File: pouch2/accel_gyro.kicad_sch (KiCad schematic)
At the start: 15 parts, among them U2 BME688, U3 BME280

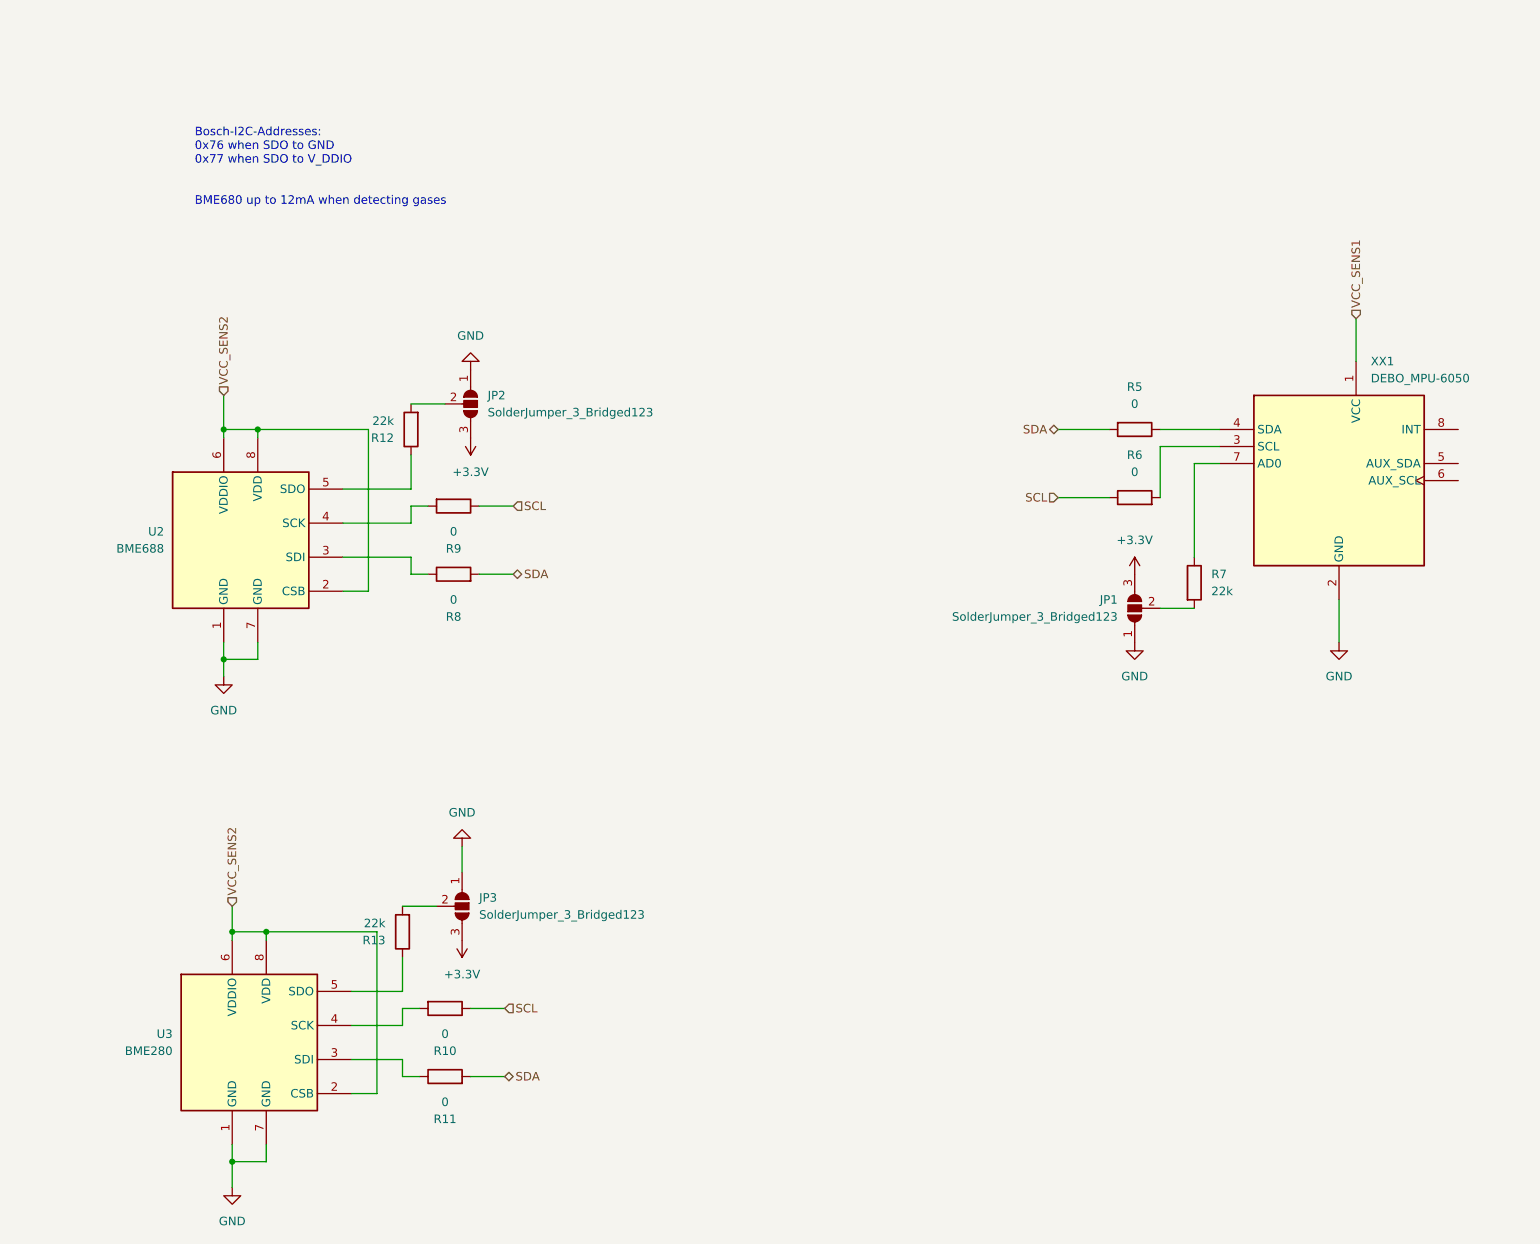
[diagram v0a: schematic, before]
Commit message: added power, sdcard
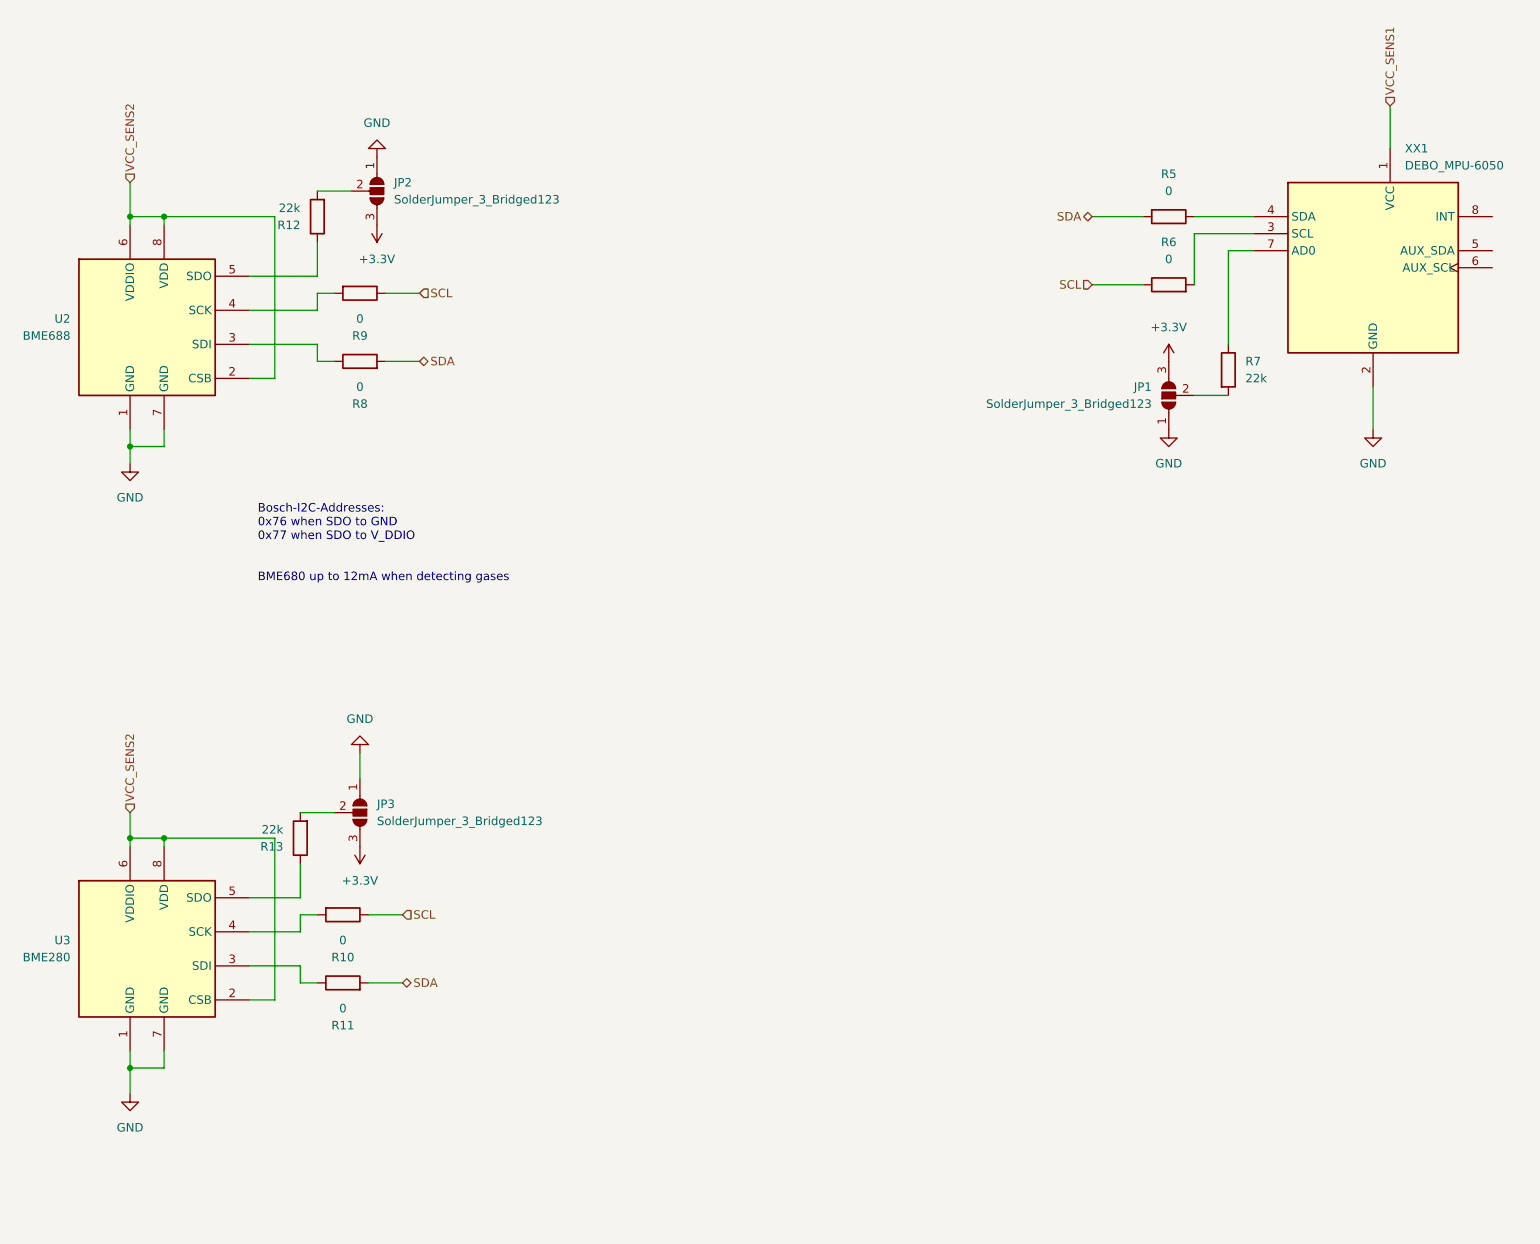
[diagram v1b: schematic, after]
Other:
- moved on the sheet: JP1, JP2, JP3, R10, R11, R12, R13, R5, R6, R7, R8, R9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

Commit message: added pi zero header
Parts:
- JP1, JP2, JP3: footprint (none) -> Jumper:SolderJumper-3_P2.0mm_Open_TrianglePad1.0x1.5mm_NumberLabels
- R10, R11, R12, R13, R5, R6, R7, R8, R9: footprint (none) -> Resistor_SMD:R_0815_2038Metric
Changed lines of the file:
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@@
 			)
 		)
-		(property "Footprint" ""
+		(property "Footprint" "Resistor_SMD:R_0815_2038Metric"
 			(at 71.12 143.002 90)
 			(effects
@@
 			)
 		)
-		(property "Footprint" ""
+		(property "Footprint" "Jumper:SolderJumper-3_P2.0mm_Open_TrianglePad1.0x1.5mm_NumberLabels"
 			(at 73.66 129.54 0)
 			(effects
@@
 			)
 		)
-		(property "Footprint" ""
+		(property "Footprint" "Jumper:SolderJumper-3_P2.0mm_Open_TrianglePad1.0x1.5mm_NumberLabels"
 			(at 194.31 67.31 0)
 			(effects
@@
 			)
 		)
-		(property "Footprint" ""
+		(property "Footprint" "Resistor_SMD:R_0815_2038Metric"
 			(at 194.31 52.578 90)
 			(effects
@@
 			)
 		)
-		(property "Footprint" ""
+		(property "Footprint" "Resistor_SMD:R_0815_2038Metric"
 			(at 71.12 156.718 90)
 			(effects
@@
 			)
 		)
-		(property "Footprint" ""
+		(property "Footprint" "Jumper:SolderJumper-3_P2.0mm_Open_TrianglePad1.0x1.5mm_NumberLabels"
 			(at 76.2 36.83 0)
 			(effects
@@
 			)
 		)
-		(property "Footprint" ""
+		(property "Footprint" "Resistor_SMD:R_0815_2038Metric"
 			(at 73.66 64.008 90)
 			(effects
@@
 			)
 		)
-		(property "Footprint" ""
+		(property "Footprint" "Resistor_SMD:R_0815_2038Metric"
 			(at 69.088 40.64 90)
 			(effects
@@
 			)
 		)
-		(property "Footprint" ""
+		(property "Footprint" "Resistor_SMD:R_0815_2038Metric"
 			(at 73.66 50.292 90)
 			(effects
@@
 			)
 		)
-		(property "Footprint" ""
+		(property "Footprint" "Resistor_SMD:R_0815_2038Metric"
 			(at 194.31 38.862 90)
 			(effects
@@
 			)
 		)
-		(property "Footprint" ""
+		(property "Footprint" "Resistor_SMD:R_0815_2038Metric"
 			(at 66.548 133.35 90)
 			(effects
@@
 			)
 		)
-		(property "Footprint" ""
+		(property "Footprint" "Resistor_SMD:R_0815_2038Metric"
 			(at 201.422 63.5 90)
 			(effects

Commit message: started PCB design
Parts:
- R201: renamed from R13; footprint Resistor_SMD:R_0815_2038Metric -> Resistor_SMD:R_0805_2012Metric
- R202: renamed from R12; footprint Resistor_SMD:R_0815_2038Metric -> Resistor_SMD:R_0805_2012Metric
- R203: renamed from R10; footprint Resistor_SMD:R_0815_2038Metric -> Resistor_SMD:R_0805_2012Metric
- R204: renamed from R11; footprint Resistor_SMD:R_0815_2038Metric -> Resistor_SMD:R_0805_2012Metric
- R205: renamed from R9; footprint Resistor_SMD:R_0815_2038Metric -> Resistor_SMD:R_0805_2012Metric
- R206: renamed from R8; footprint Resistor_SMD:R_0815_2038Metric -> Resistor_SMD:R_0805_2012Metric
- R207: renamed from R5; footprint Resistor_SMD:R_0815_2038Metric -> Resistor_SMD:R_0805_2012Metric
- R208: renamed from R6; footprint Resistor_SMD:R_0815_2038Metric -> Resistor_SMD:R_0805_2012Metric
- R209: renamed from R7; footprint Resistor_SMD:R_0815_2038Metric -> Resistor_SMD:R_0805_2012Metric
- renumbered JP3 to JP201, JP2 to JP202, JP1 to JP203, U2 to U201, U3 to U202, XX1 to XX201
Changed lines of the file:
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@@
 		(dnp no)
 		(fields_autoplaced yes)
-		(property "Reference" "R10"
+		(property "Reference" "R203"
 			(at 71.12 151.13 90)
 			(effects
@@
 			)
 		)
-		(property "Footprint" "Resistor_SMD:R_0815_2038Metric"
+		(property "Footprint" "Resistor_SMD:R_0805_2012Metric"
 			(at 71.12 143.002 90)
 			(effects
@@
 			(project "pouch2"
 				(path "/278cfa6b-9496-4a22-b425-8abdb96793ef/245dc3ad-3701-4382-b188-f6e1df98764a"
-					(reference "R10")
+					(reference "R203")
 					(unit 1)
 				)
@@
 		(dnp no)
 		(fields_autoplaced yes)
-		(property "Reference" "JP3"
+		(property "Reference" "JP201"
 			(at 76.2 128.2699 90)
 			(effects
@@
 			(project "pouch2"
 				(path "/278cfa6b-9496-4a22-b425-8abdb96793ef/245dc3ad-3701-4382-b188-f6e1df98764a"
-					(reference "JP3")
+					(reference "JP201")
 					(unit 1)
 				)
@@
 		(dnp no)
 		(fields_autoplaced yes)
-		(property "Reference" "#PWR012"
+		(property "Reference" "#PWR0204"
 			(at 73.66 130.81 0)
 			(effects
@@
 			(project "pouch2"
 				(path "/278cfa6b-9496-4a22-b425-8abdb96793ef/245dc3ad-3701-4382-b188-f6e1df98764a"
-					(reference "#PWR012")
+					(reference "#PWR0204")
 					(unit 1)
 				)
@@
 		(dnp no)
 		(fields_autoplaced yes)
-		(property "Reference" "JP1"
+		(property "Reference" "JP203"
 			(at 191.77 66.0399 90)
 			(effects
@@
 			(project "pouch2"
 				(path "/278cfa6b-9496-4a22-b425-8abdb96793ef/245dc3ad-3701-4382-b188-f6e1df98764a"
-					(reference "JP1")
+					(reference "JP203")
 					(unit 1)
 				)
@@
 		(dnp no)
 		(fields_autoplaced yes)
-		(property "Reference" "#PWR02"
+		(property "Reference" "#PWR0208"
 			(at 194.31 78.74 0)
 			(effects
@@
 			(project "pouch2"
 				(path "/278cfa6b-9496-4a22-b425-8abdb96793ef/245dc3ad-3701-4382-b188-f6e1df98764a"
-					(reference "#PWR02")
+					(reference "#PWR0208")
 					(unit 1)
 				)
@@
 		(dnp no)
 		(fields_autoplaced yes)
-		(property "Reference" "R6"
+		(property "Reference" "R208"
 			(at 194.31 44.45 90)
 			(effects
@@
 			)
 		)
-		(property "Footprint" "Resistor_SMD:R_0815_2038Metric"
+		(property "Footprint" "Resistor_SMD:R_0805_2012Metric"
 			(at 194.31 52.578 90)
 			(effects
@@
 			(project "pouch2"
 				(path "/278cfa6b-9496-4a22-b425-8abdb96793ef/245dc3ad-3701-4382-b188-f6e1df98764a"
-					(reference "R6")
+					(reference "R208")
 					(unit 1)
 				)
@@
 		(dnp no)
 		(fields_autoplaced yes)
-		(property "Reference" "U2"
+		(property "Reference" "U201"
 			(at 30.48 55.8799 0)
 			(effects
@@
 			(project ""
 				(path "/278cfa6b-9496-4a22-b425-8abdb96793ef/245dc3ad-3701-4382-b188-f6e1df98764a"
-					(reference "U2")
+					(reference "U201")
 					(unit 1)
 				)
@@
 		(dnp no)
 		(fields_autoplaced yes)
-		(property "Reference" "R11"
+		(property "Reference" "R204"
 			(at 71.12 161.29 90)
 			(effects
@@
 			)
 		)
-		(property "Footprint" "Resistor_SMD:R_0815_2038Metric"
+		(property "Footprint" "Resistor_SMD:R_0805_2012Metric"
 			(at 71.12 156.718 90)
 			(effects
@@
 			(project "pouch2"
 				(path "/278cfa6b-9496-4a22-b425-8abdb96793ef/245dc3ad-3701-4382-b188-f6e1df98764a"
-					(reference "R11")
+					(reference "R204")
 					(unit 1)
 				)
@@
 		(dnp no)
 		(fields_autoplaced yes)
-		(property "Reference" "#PWR05"
+		(property "Reference" "#PWR0209"
 			(at 224.79 78.74 0)
 			(effects
@@
 			(project "pouch2"
 				(path "/278cfa6b-9496-4a22-b425-8abdb96793ef/245dc3ad-3701-4382-b188-f6e1df98764a"
-					(reference "#PWR05")
+					(reference "#PWR0209")
 					(unit 1)
 				)
@@
 		(dnp no)
 		(fields_autoplaced yes)
-		(property "Reference" "JP2"
+		(property "Reference" "JP202"
 			(at 78.74 35.5599 90)
 			(effects
@@
 			(project "pouch2"
 				(path "/278cfa6b-9496-4a22-b425-8abdb96793ef/245dc3ad-3701-4382-b188-f6e1df98764a"
-					(reference "JP2")
+					(reference "JP202")
 					(unit 1)
 				)
@@
 		(dnp no)
 		(fields_autoplaced yes)
-		(property "Reference" "XX1"
+		(property "Reference" "XX201"
 			(at 229.5241 30.48 0)
 			(effects
@@
 			(project "pouch2"
 				(path "/278cfa6b-9496-4a22-b425-8abdb96793ef/245dc3ad-3701-4382-b188-f6e1df98764a"
-					(reference "XX1")
+					(reference "XX201")
 					(unit 1)
 				)
@@
 		(dnp no)
 		(fields_autoplaced yes)
-		(property "Reference" "#PWR011"
+		(property "Reference" "#PWR0203"
 			(at 73.66 114.3 0)
 			(effects
@@
 			(project "pouch2"
 				(path "/278cfa6b-9496-4a22-b425-8abdb96793ef/245dc3ad-3701-4382-b188-f6e1df98764a"
-					(reference "#PWR011")
+					(reference "#PWR0203")
 					(unit 1)
 				)
@@
 		(dnp no)
 		(fields_autoplaced yes)
-		(property "Reference" "R8"
+		(property "Reference" "R206"
 			(at 73.66 68.58 90)
 			(effects
@@
 			)
 		)
-		(property "Footprint" "Resistor_SMD:R_0815_2038Metric"
+		(property "Footprint" "Resistor_SMD:R_0805_2012Metric"
 			(at 73.66 64.008 90)
 			(effects
@@
 			(project "pouch2"
 				(path "/278cfa6b-9496-4a22-b425-8abdb96793ef/245dc3ad-3701-4382-b188-f6e1df98764a"
-					(reference "R8")
+					(reference "R206")
 					(unit 1)
 				)
@@
 		(dnp no)
 		(fields_autoplaced yes)
-		(property "Reference" "R12"
+		(property "Reference" "R202"
 			(at 64.77 41.9101 0)
 			(effects
@@
 			)
 		)
-		(property "Footprint" "Resistor_SMD:R_0815_2038Metric"
+		(property "Footprint" "Resistor_SMD:R_0805_2012Metric"
 			(at 69.088 40.64 90)
 			(effects
@@
 			(project "pouch2"
 				(path "/278cfa6b-9496-4a22-b425-8abdb96793ef/245dc3ad-3701-4382-b188-f6e1df98764a"
-					(reference "R12")
+					(reference "R202")
 					(unit 1)
 				)
@@
 		(dnp no)
 		(fields_autoplaced yes)
-		(property "Reference" "R9"
+		(property "Reference" "R205"
 			(at 73.66 58.42 90)
 			(effects
@@
 			)
 		)
-		(property "Footprint" "Resistor_SMD:R_0815_2038Metric"
+		(property "Footprint" "Resistor_SMD:R_0805_2012Metric"
 			(at 73.66 50.292 90)
 			(effects
@@
 			(project "pouch2"
 				(path "/278cfa6b-9496-4a22-b425-8abdb96793ef/245dc3ad-3701-4382-b188-f6e1df98764a"
-					(reference "R9")
+					(reference "R205")
 					(unit 1)
 				)
@@
 		(dnp no)
 		(fields_autoplaced yes)
-		(property "Reference" "R5"
+		(property "Reference" "R207"
 			(at 194.31 34.29 90)
 			(effects
@@
 			)
 		)
-		(property "Footprint" "Resistor_SMD:R_0815_2038Metric"
+		(property "Footprint" "Resistor_SMD:R_0805_2012Metric"
 			(at 194.31 38.862 90)
 			(effects
@@
 			(project "pouch2"
 				(path "/278cfa6b-9496-4a22-b425-8abdb96793ef/245dc3ad-3701-4382-b188-f6e1df98764a"
-					(reference "R5")
+					(reference "R207")
 					(unit 1)
 				)
@@
 		(dnp no)
 		(fields_autoplaced yes)
-		(property "Reference" "R13"
+		(property "Reference" "R201"
 			(at 62.23 134.6201 0)
 			(effects
@@
 			)
 		)
-		(property "Footprint" "Resistor_SMD:R_0815_2038Metric"
+		(property "Footprint" "Resistor_SMD:R_0805_2012Metric"
 			(at 66.548 133.35 90)
 			(effects
@@
 			(project "pouch2"
 				(path "/278cfa6b-9496-4a22-b425-8abdb96793ef/245dc3ad-3701-4382-b188-f6e1df98764a"
-					(reference "R13")
+					(reference "R201")
 					(unit 1)
 				)
@@
 		(dnp no)
 		(fields_autoplaced yes)
-		(property "Reference" "#PWR07"
+		(property "Reference" "#PWR0201"
 			(at 39.37 83.82 0)
 			(effects
@@
 			(project ""
 				(path "/278cfa6b-9496-4a22-b425-8abdb96793ef/245dc3ad-3701-4382-b188-f6e1df98764a"
-					(reference "#PWR07")
+					(reference "#PWR0201")
 					(unit 1)
 				)
@@
 		(dnp no)
 		(fields_autoplaced yes)
-		(property "Reference" "#PWR08"
+		(property "Reference" "#PWR0202"
 			(at 39.37 177.8 0)
 			(effects
@@
 			(project ""
 				(path "/278cfa6b-9496-4a22-b425-8abdb96793ef/245dc3ad-3701-4382-b188-f6e1df98764a"
-					(reference "#PWR08")
+					(reference "#PWR0202")
 					(unit 1)
 				)
@@
 		(dnp no)
 		(fields_autoplaced yes)
-		(property "Reference" "U3"
+		(property "Reference" "U202"
 			(at 30.48 148.5899 0)
 			(effects
@@
 			(project ""
 				(path "/278cfa6b-9496-4a22-b425-8abdb96793ef/245dc3ad-3701-4382-b188-f6e1df98764a"
-					(reference "U3")
+					(reference "U202")
 					(unit 1)
 				)
@@
 		(dnp no)
 		(fields_autoplaced yes)
-		(property "Reference" "#PWR010"
+		(property "Reference" "#PWR0205"
 			(at 76.2 25.4 0)
 			(effects
@@
 			(project "pouch2"
 				(path "/278cfa6b-9496-4a22-b425-8abdb96793ef/245dc3ad-3701-4382-b188-f6e1df98764a"
-					(reference "#PWR010")
+					(reference "#PWR0205")
 					(unit 1)
 				)
@@
 		(dnp no)
 		(fields_autoplaced yes)
-		(property "Reference" "R7"
+		(property "Reference" "R209"
 			(at 205.74 62.2299 0)
 			(effects
@@
 			)
 		)
-		(property "Footprint" "Resistor_SMD:R_0815_2038Metric"
+		(property "Footprint" "Resistor_SMD:R_0805_2012Metric"
 			(at 201.422 63.5 90)
 			(effects
@@
 			(project "pouch2"
 				(path "/278cfa6b-9496-4a22-b425-8abdb96793ef/245dc3ad-3701-4382-b188-f6e1df98764a"
-					(reference "R7")
+					(reference "R209")
 					(unit 1)
 				)
@@
 		(dnp no)
 		(fields_autoplaced yes)
-		(property "Reference" "#PWR01"
+		(property "Reference" "#PWR0207"
 			(at 194.31 66.04 0)
 			(effects
@@
 			(project "pouch2"
 				(path "/278cfa6b-9496-4a22-b425-8abdb96793ef/245dc3ad-3701-4382-b188-f6e1df98764a"
-					(reference "#PWR01")
+					(reference "#PWR0207")
 					(unit 1)
 				)
@@
 		(dnp no)
 		(fields_autoplaced yes)
-		(property "Reference" "#PWR09"
+		(property "Reference" "#PWR0206"
 			(at 76.2 38.1 0)
 			(effects
@@
 			(project "pouch2"
 				(path "/278cfa6b-9496-4a22-b425-8abdb96793ef/245dc3ad-3701-4382-b188-f6e1df98764a"
-					(reference "#PWR09")
-					(unit 1)
-				)
+					(reference "#PWR0206")
+					(unit 1)
+				)

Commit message: updated backside of PCB
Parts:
- XX201: footprint SensorBoards:DEBO_MPU-6050_Board -> SensorBoards:DEBO_MPU6050
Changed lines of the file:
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@@
 			)
 		)
-		(property "Footprint" "SensorBoards:DEBO_MPU-6050_Board"
+		(property "Footprint" "SensorBoards:DEBO_MPU6050"
 			(at 224.79 68.58 0)
 			(effects

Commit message: started routing
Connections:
- net SCL: now also R203.2; no longer R203.1
- net at U202.4 (SCK): now also R203.1; no longer R203.2
- net at U201.5 (SDO): now also R202.2; no longer R202.1
- net at JP202.2 (C): now also R202.1; no longer R202.2
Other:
- moved on the sheet: JP201, JP202, JP203, R201, R202, R203, R204, R205, R206, R207, R208, R209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
